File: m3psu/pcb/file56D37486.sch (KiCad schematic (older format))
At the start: 44 parts

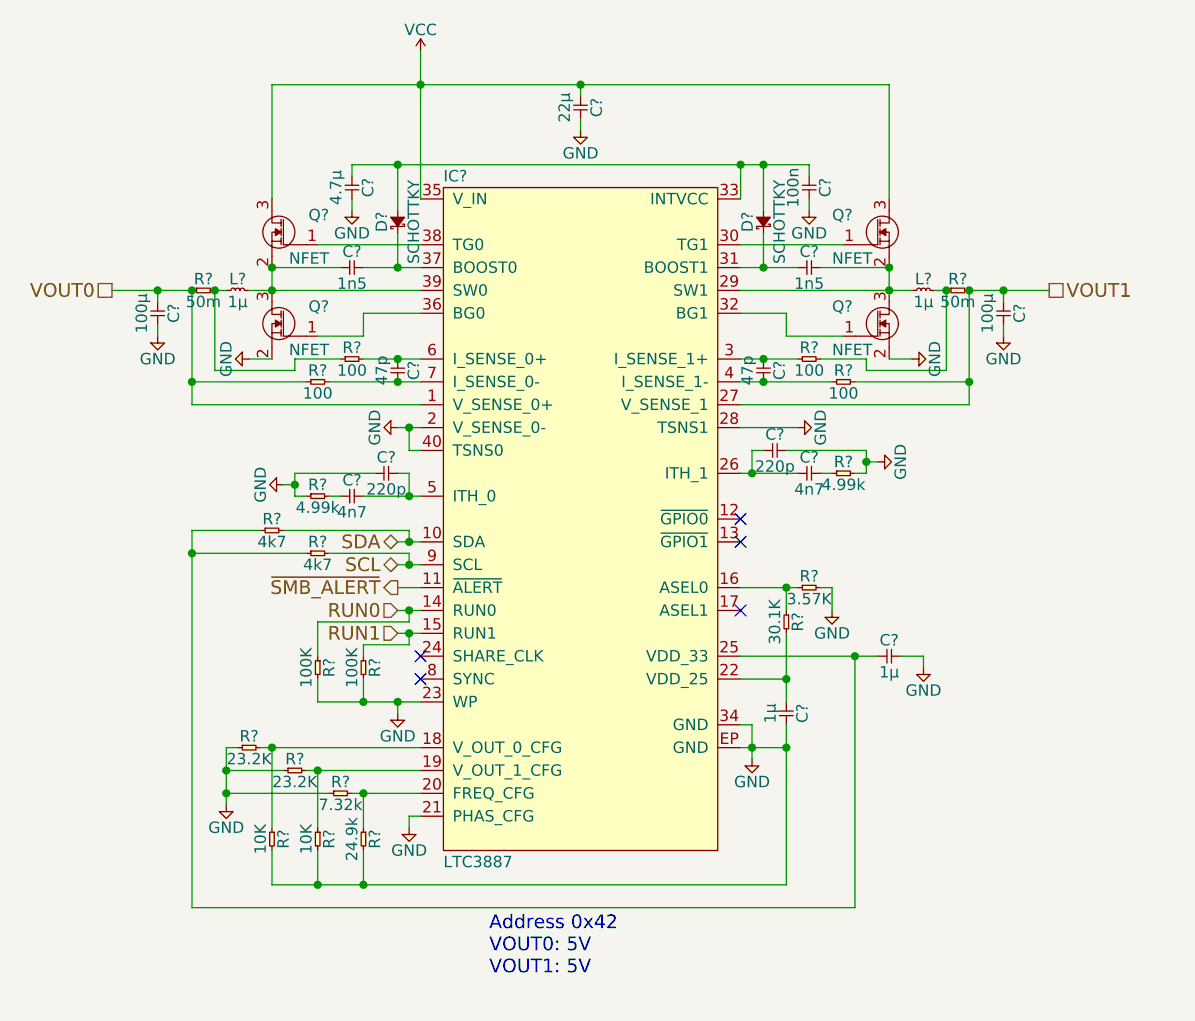
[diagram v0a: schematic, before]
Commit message: Finished passives for Li-ion Charger. Tweaked and cleaned up values in DC/DC Converter.
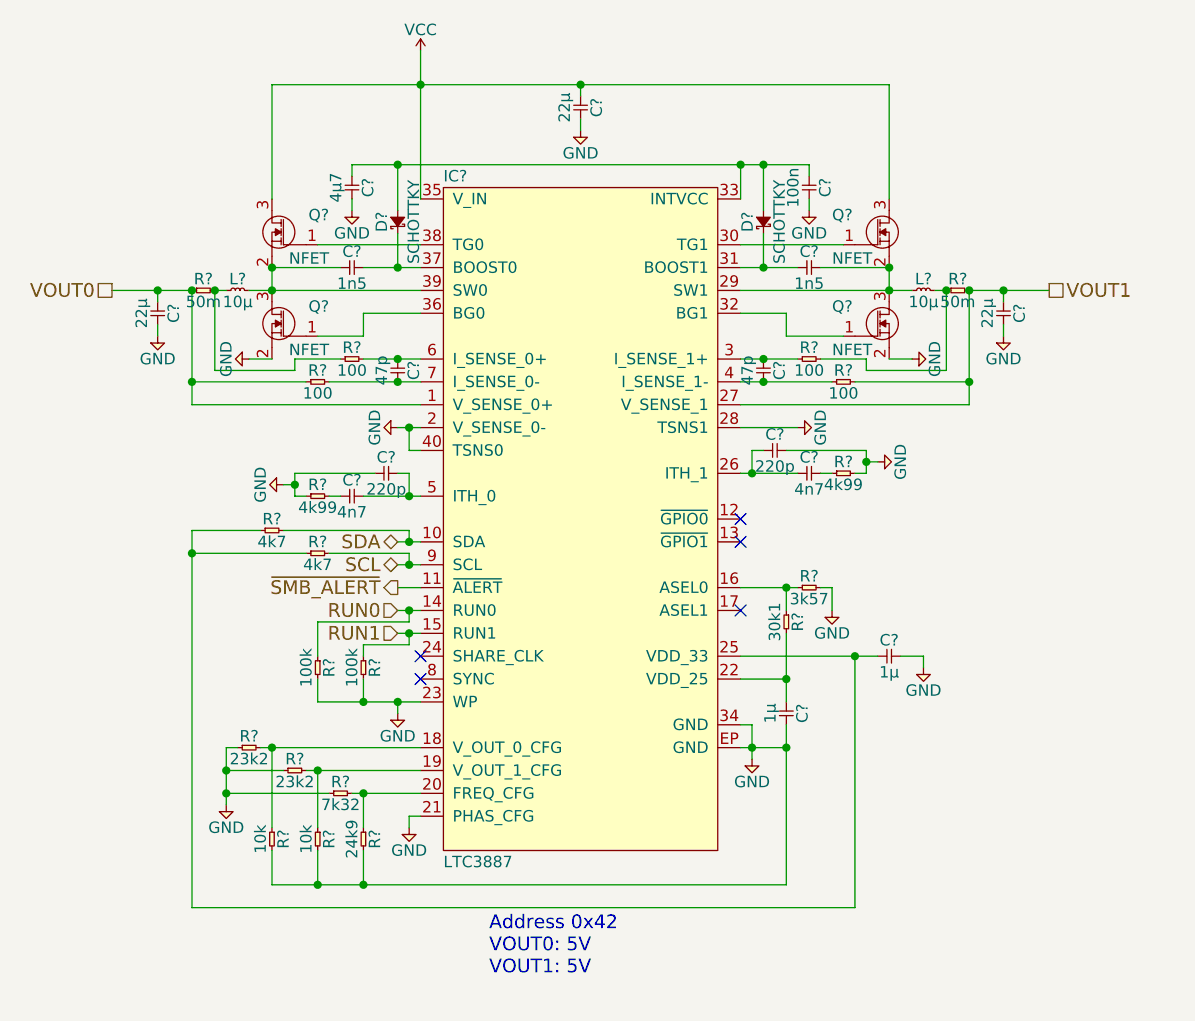
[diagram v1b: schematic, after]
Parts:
- C?: value 4.7µ -> 4µ7
- C? (x2): value 100µ -> 22µ; Farnell 1735535 -> 2494232
- L? (x2): value 1µ -> 10µ; Farnell 2292535 -> 2292532
- R?: value 24.9k -> 24k9
- R? (x2): value 10K -> 10k
- R? (x2): value 23.2K -> 23k2
- R?: value 7.32k -> 7k32
- R?: value 3.57K -> 3k57
- R?: value 30.1K -> 30k1
- R? (x2): value 4.99k -> 4k99
- R? (x2): value 100K -> 100k
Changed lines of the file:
@@
 P 7100 2850
 F 0 "L?" H 7150 2900 50  0000 C CNN
-F 1 "1µ" H 7150 2800 50  0000 C CNN
+F 1 "10µ" H 7150 2800 50  0000 C CNN
 F 2 "" H 7100 2850 50  0001 C CNN
 F 3 "" H 7100 2850 50  0001 C CNN
-F 4 "2292535" H 7100 2850 60  0001 C CNN "Farnell"
+F 4 "2292532" H 7100 2850 60  0001 C CNN "Farnell"
 	1    7100 2850
 	1    0    0    -1
@@
 P 4100 2850
 F 0 "L?" H 4150 2900 50  0000 C CNN
-F 1 "1µ" H 4150 2800 50  0000 C CNN
+F 1 "10µ" H 4150 2800 50  0000 C CNN
 F 2 "" H 4100 2850 50  0001 C CNN
 F 3 "" H 4100 2850 50  0001 C CNN
-F 4 "2292535" H 4100 2850 60  0001 C CNN "Farnell"
+F 4 "2292532" H 4100 2850 60  0001 C CNN "Farnell"
 	1    4100 2850
 	1    0    0    -1
@@
 P 4650 2350
 F 0 "C?" H 4700 2420 50  0000 C CNN
-F 1 "4.7µ" H 4700 2280 50  0000 C CNN
+F 1 "4µ7" H 4700 2280 50  0000 C CNN
 F 2 "" H 4650 2350 50  0001 C CNN
 F 3 "" H 4650 2350 50  0001 C CNN
@@
 P 7500 2900
 F 0 "C?" H 7550 2970 50  0000 C CNN
-F 1 "100µ" H 7550 2830 50  0000 C CNN
+F 1 "22µ" H 7550 2830 50  0000 C CNN
 F 2 "" H 7500 2900 50  0001 C CNN
 F 3 "" H 7500 2900 50  0001 C CNN
-F 4 "1735535" H 7500 2900 60  0001 C CNN "Farnell"
+F 4 "2494232" H 7500 2900 60  0001 C CNN "Farnell"
 	1    7500 2900
 	0    1    1    0
@@
 P 3800 2900
 F 0 "C?" H 3850 2970 50  0000 C CNN
-F 1 "100µ" H 3850 2830 50  0000 C CNN
+F 1 "22µ" H 3850 2830 50  0000 C CNN
 F 2 "" H 3800 2900 50  0001 C CNN
 F 3 "" H 3800 2900 50  0001 C CNN
-F 4 "1735535" H 3800 2900 60  0001 C CNN "Farnell"
+F 4 "2494232" H 3800 2900 60  0001 C CNN "Farnell"
 	1    3800 2900
 	0    1    1    0
@@
 P 4700 5200
 F 0 "R?" H 4750 5250 50  0000 C CNN
-F 1 "24.9k" H 4750 5150 50  0000 C CNN
+F 1 "24k9" H 4750 5150 50  0000 C CNN
 F 2 "" H 4700 5200 50  0001 C CNN
 F 3 "" H 4700 5200 50  0001 C CNN
@@
 P 4500 5200
 F 0 "R?" H 4550 5250 50  0000 C CNN
-F 1 "10K" H 4550 5150 50  0000 C CNN
+F 1 "10k" H 4550 5150 50  0000 C CNN
 F 2 "" H 4500 5200 50  0001 C CNN
 F 3 "" H 4500 5200 50  0001 C CNN
@@
 P 4300 5200
 F 0 "R?" H 4350 5250 50  0000 C CNN
-F 1 "10K" H 4350 5150 50  0000 C CNN
+F 1 "10k" H 4350 5150 50  0000 C CNN
 F 2 "" H 4300 5200 50  0001 C CNN
 F 3 "" H 4300 5200 50  0001 C CNN
@@
 P 4150 4850
 F 0 "R?" H 4200 4900 50  0000 C CNN
-F 1 "23.2K" H 4200 4800 50  0000 C CNN
+F 1 "23k2" H 4200 4800 50  0000 C CNN
 F 2 "" H 4150 4850 50  0001 C CNN
 F 3 "" H 4150 4850 50  0001 C CNN
@@
 P 4350 4950
 F 0 "R?" H 4400 5000 50  0000 C CNN
-F 1 "23.2K" H 4400 4900 50  0000 C CNN
+F 1 "23k2" H 4400 4900 50  0000 C CNN
 F 2 "" H 4350 4950 50  0001 C CNN
 F 3 "" H 4350 4950 50  0001 C CNN
@@
 P 4550 5050
 F 0 "R?" H 4600 5100 50  0000 C CNN
-F 1 "7.32k" H 4600 5000 50  0000 C CNN
+F 1 "7k32" H 4600 5000 50  0000 C CNN
 F 2 "" H 4550 5050 50  0001 C CNN
 F 3 "" H 4550 5050 50  0001 C CNN
@@
 P 6600 4150
 F 0 "R?" H 6650 4200 50  0000 C CNN
-F 1 "3.57K" H 6650 4100 50  0000 C CNN
+F 1 "3k57" H 6650 4100 50  0000 C CNN
 F 2 "" H 6600 4150 50  0001 C CNN
 F 3 "" H 6600 4150 50  0001 C CNN
@@
 P 6550 4250
 F 0 "R?" H 6600 4300 50  0000 C CNN
-F 1 "30.1K" H 6600 4200 50  0000 C CNN
+F 1 "30k1" H 6600 4200 50  0000 C CNN
 F 2 "" H 6550 4250 50  0001 C CNN
 F 3 "" H 6550 4250 50  0001 C CNN
@@
 P 6750 3650
 F 0 "R?" H 6800 3700 50  0000 C CNN
-F 1 "4.99k" H 6800 3600 50  0000 C CNN
+F 1 "4k99" H 6800 3600 50  0000 C CNN
 F 2 "" H 6750 3650 50  0001 C CNN
 F 3 "" H 6750 3650 50  0001 C CNN
@@
 P 4450 3750
 F 0 "R?" H 4500 3800 50  0000 C CNN
-F 1 "4.99k" H 4500 3700 50  0000 C CNN
+F 1 "4k99" H 4500 3700 50  0000 C CNN
 F 2 "" H 4450 3750 50  0001 C CNN
 F 3 "" H 4450 3750 50  0001 C CNN
@@
 P 4700 4450
 F 0 "R?" H 4750 4500 50  0000 C CNN
-F 1 "100K" H 4750 4400 50  0000 C CNN
+F 1 "100k" H 4750 4400 50  0000 C CNN
 F 2 "" H 4700 4450 50  0001 C CNN
 F 3 "" H 4700 4450 50  0001 C CNN
@@
 P 4500 4450
 F 0 "R?" H 4550 4500 50  0000 C CNN
-F 1 "100K" H 4550 4400 50  0000 C CNN
+F 1 "100k" H 4550 4400 50  0000 C CNN
 F 2 "" H 4500 4450 50  0001 C CNN
 F 3 "" H 4500 4450 50  0001 C CNN

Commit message: Linked the footprints to some parts. Cleaned up a little more of DC/DC Converter.
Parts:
- C?: footprint (none) -> agg:0603
- C?: Farnell (none) -> 2494232
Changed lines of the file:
@@
 F 0 "C?" H 4700 2420 50  0000 C CNN
 F 1 "4µ7" H 4700 2280 50  0000 C CNN
-F 2 "" H 4650 2350 50  0001 C CNN
+F 2 "agg:0603" H 4650 2350 50  0001 C CNN
 F 3 "" H 4650 2350 50  0001 C CNN
 	1    4650 2350
@@
 F 2 "" H 5650 2000 50  0001 C CNN
 F 3 "" H 5650 2000 50  0001 C CNN
+F 4 "2494232" H 5650 2000 60  0001 C CNN "Farnell"
 	1    5650 2000
 	0    1    1    0

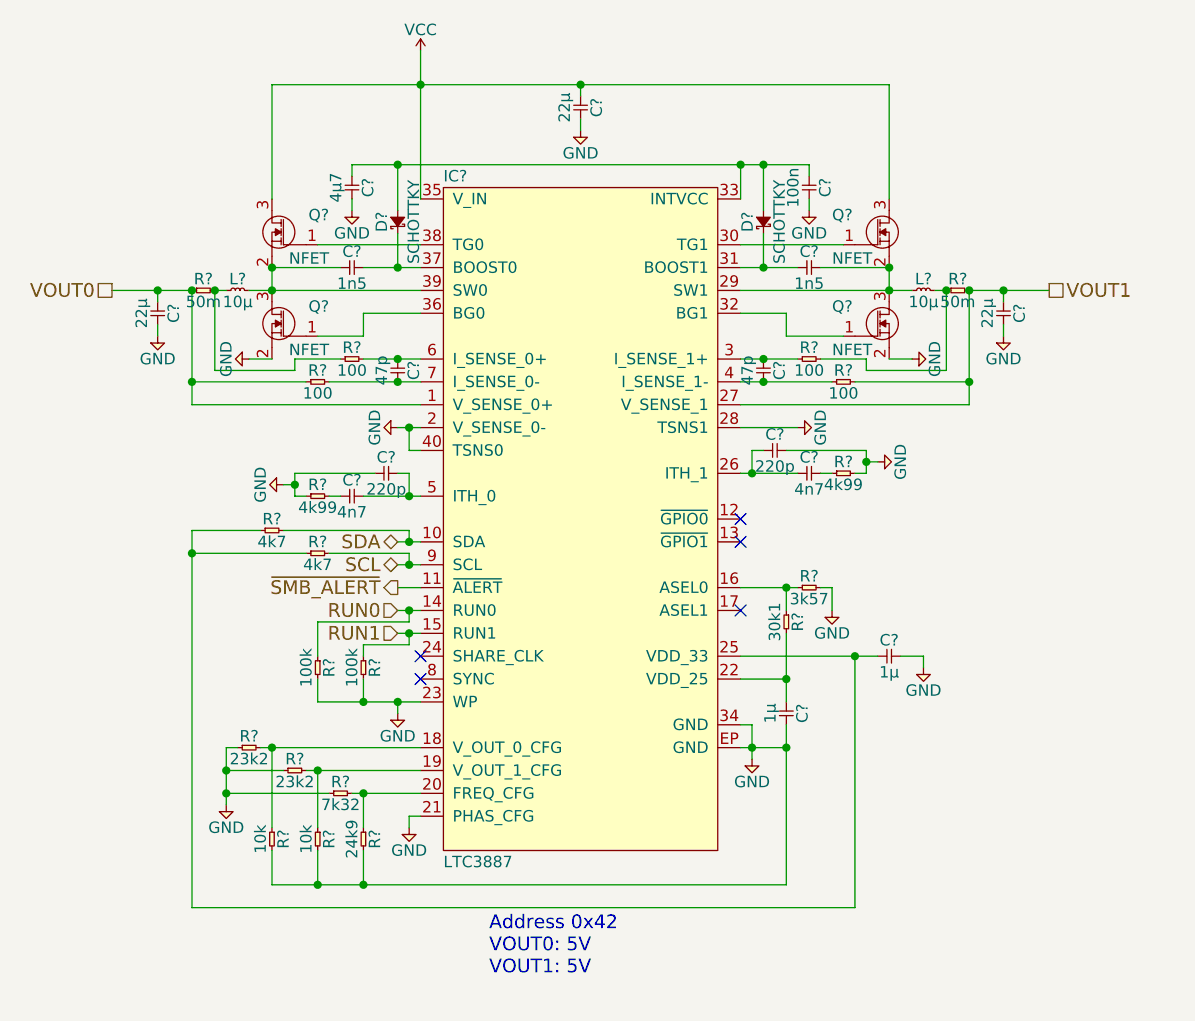
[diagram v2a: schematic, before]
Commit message: Add farnell numbers and footprints to dc converter parts
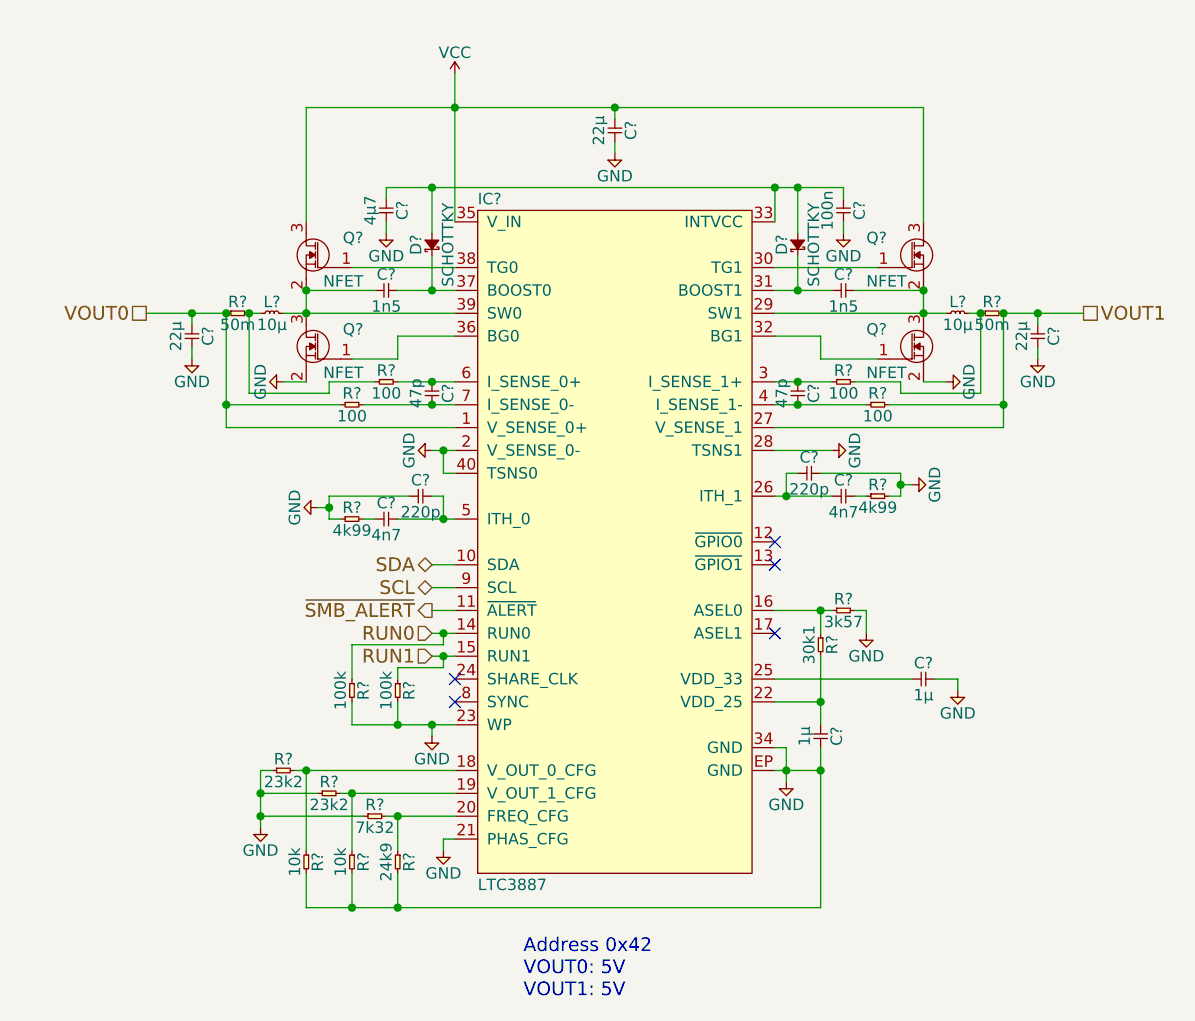
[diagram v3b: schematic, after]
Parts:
- removed C? (x2): 1n5, symbol C
- removed C?: 4µ7, agg:0603, symbol C
- removed C? (x3): 22µ, symbol C
- removed C? (x2): 47p, symbol C
- removed C? (x2): 1µ, symbol C
- removed C?: 100n, symbol C
- removed C? (x2): 4n7, symbol C
- removed C? (x2): 220p, symbol C
- removed D? (x2): SCHOTTKY, symbol SCHOTTKY
- removed IC?: LTC3887, agg:QFN-40-EP-LTC-UJ, symbol LTC3887
- removed L? (x2): 10µ, symbol L
- removed Q? (x4): NFET, symbol NFET
- removed R? (x2): 50m, symbol R
- removed R? (x4): 100, symbol R
- removed R?: 24k9, symbol R
- removed R? (x2): 10k, symbol R
- removed R? (x2): 23k2, symbol R
- removed R?: 7k32, symbol R
- removed R?: 3k57, symbol R
- removed R?: 30k1, symbol R
- removed R? (x2): 4k7, symbol R
- removed R? (x2): 4k99, symbol R
- removed R? (x2): 100k, symbol R
- added C? (x2): 1n5, agg:0402, symbol C
- added C?: 4µ7, agg:0603, symbol C
- added C? (x3): 22µ, agg:0603, symbol C
- added C? (x2): 47p, agg:0402, symbol C
- added C? (x2): 1µ, agg:0402, symbol C
- added C?: 100n, agg:0402, symbol C
- added C? (x2): 4n7, agg:0402, symbol C
- added C? (x2): 220p, agg:0402, symbol C
- added D? (x2): SCHOTTKY, agg:0603-LED, symbol SCHOTTKY
- added IC?: LTC3887, agg:QFN-40-EP-LTC-UJ, symbol LTC3887
- added L? (x2): 10µ, agg:TYS5040, symbol L
- added Q? (x4): NFET, symbol NFET
- added R? (x2): 50m, agg:0603, symbol R
- added R? (x4): 100, agg:0402, symbol R
- added R?: 24k9, agg:0402, symbol R
- added R? (x2): 10k, agg:0402, symbol R
- added R? (x2): 23k2, agg:0402, symbol R
- added R?: 7k32, agg:0402, symbol R
- added R?: 3k57, agg:0402, symbol R
- added R?: 30k1, agg:0402, symbol R
- added R? (x2): 4k99, agg:0402, symbol R
- added R? (x2): 100k, agg:0402, symbol R
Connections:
- net GND: now also C?.1, C?.2, C?.2, C?.2, C?.2, C?.2, C?.2, C?.2, C?.2, IC?.2 (V_SENSE_0-), IC?.21 (PHAS_CFG), IC?.23 (WP), IC?.28 (TSNS1), IC?.34 (GND), IC?.40 (TSNS0), IC?.EP (GND), Q?.2 (S), Q?.2 (S), R?.1, R?.1, R?.1, R?.1, R?.2, R?.2, R?.2, R?.2, R?.2, R?.2, R?.2
- net RUN0: now also IC?.14 (RUN0), R?.1
- net RUN1: now also IC?.15 (RUN1), R?.1
- net SCL: now also IC?.9 (SCL)
- net SDA: now also IC?.10 (SDA)
- net VCC: now also C?.1, IC?.35 (V_IN), Q?.3 (D), Q?.3 (D)
- net VOUT0: now also C?.1, IC?.1 (V_SENSE_0+), R?.1, R?.1
- net VOUT1: now also C?.1, IC?.27 (V_SENSE_1), R?.2, R?.2
- net ~SMB_ALERT: now also IC?.11 (~ALERT)
- new net: IC?.16 (ASEL0), R?.1, R?.1
- new net: IC?.18 (V_OUT_0_CFG), R?.1, R?.2
- new net: IC?.19 (V_OUT_1_CFG), R?.1, R?.2
- new net: IC?.20 (FREQ_CFG), R?.1, R?.2
- new net: C?.1, IC?.22 (VDD_25), R?.2
- new net: C?.1, IC?.25 (VDD_33)
- new net: C?.1, C?.1, IC?.26 (ITH_1)
- new net: C?.2, IC?.29 (SW1), L?.1, Q?.2 (S), Q?.3 (D)
- new net: C?.1, IC?.3 (I_SENSE_1+), R?.1
- new net: IC?.30 (TG1), Q?.1 (G)
- new net: C?.1, D?.1, IC?.31 (BOOST1)
- new net: IC?.32 (BG1), Q?.1 (G)
- new net: C?.1, C?.1, D?.2, D?.2, IC?.33 (INTVCC)
- new net: IC?.36 (BG0), Q?.1 (G)
- new net: C?.2, D?.1, IC?.37 (BOOST0)
- new net: IC?.38 (TG0), Q?.1 (G)
- new net: C?.1, IC?.39 (SW0), L?.2, Q?.2 (S), Q?.3 (D)
- new net: C?.2, IC?.4 (I_SENSE_1-), R?.1
- new net: C?.2, C?.2, IC?.5 (ITH_0)
- new net: C?.1, IC?.6 (I_SENSE_0+), R?.2
- new net: C?.2, IC?.7 (I_SENSE_0-), R?.2
- new net: L?.2, R?.1, R?.2
- new net: L?.1, R?.1, R?.2
- new net: C?.2, R?.1
- new net: C?.1, R?.2
